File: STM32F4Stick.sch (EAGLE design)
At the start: 46 parts, among them U1 MIC5219 3.3V, U2 USD-SOCKETNEW

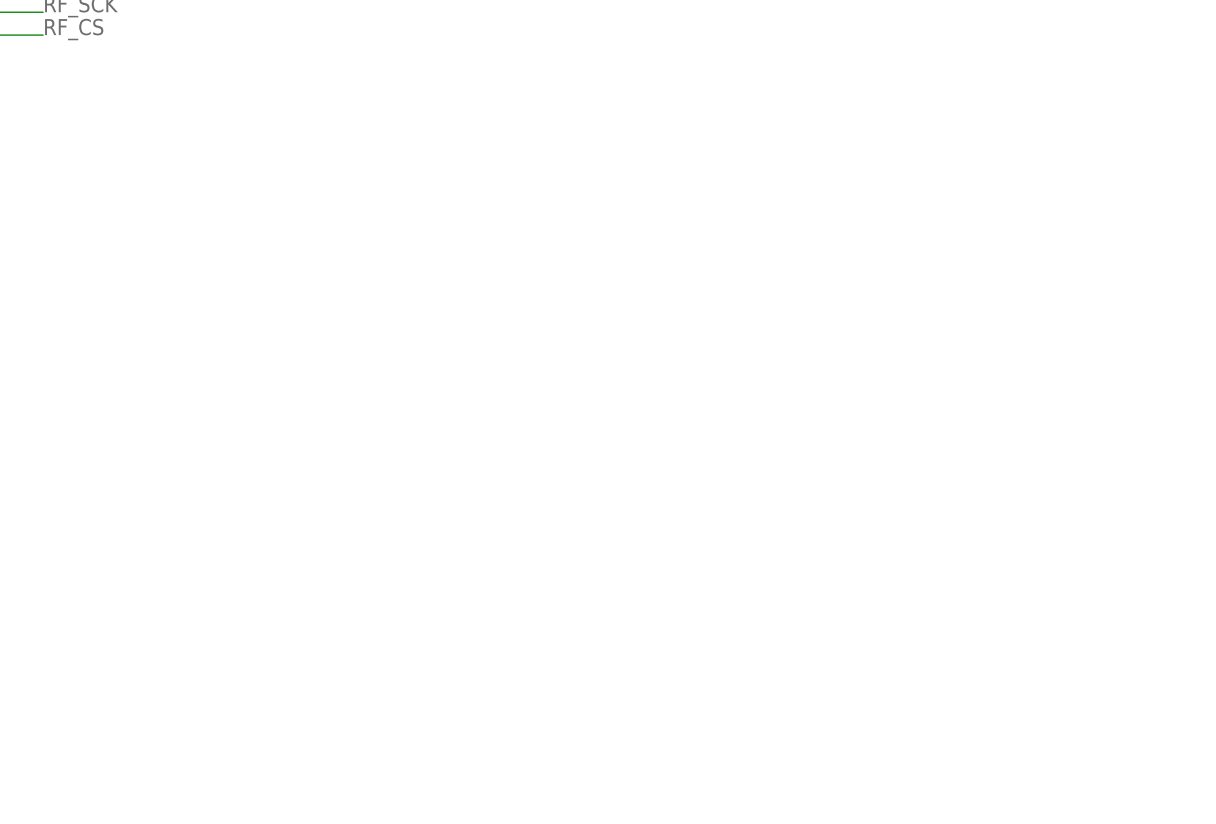
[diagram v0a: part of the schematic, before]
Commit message: version 3 still in development. playing with mpu6050/9150 module to see if one can fit
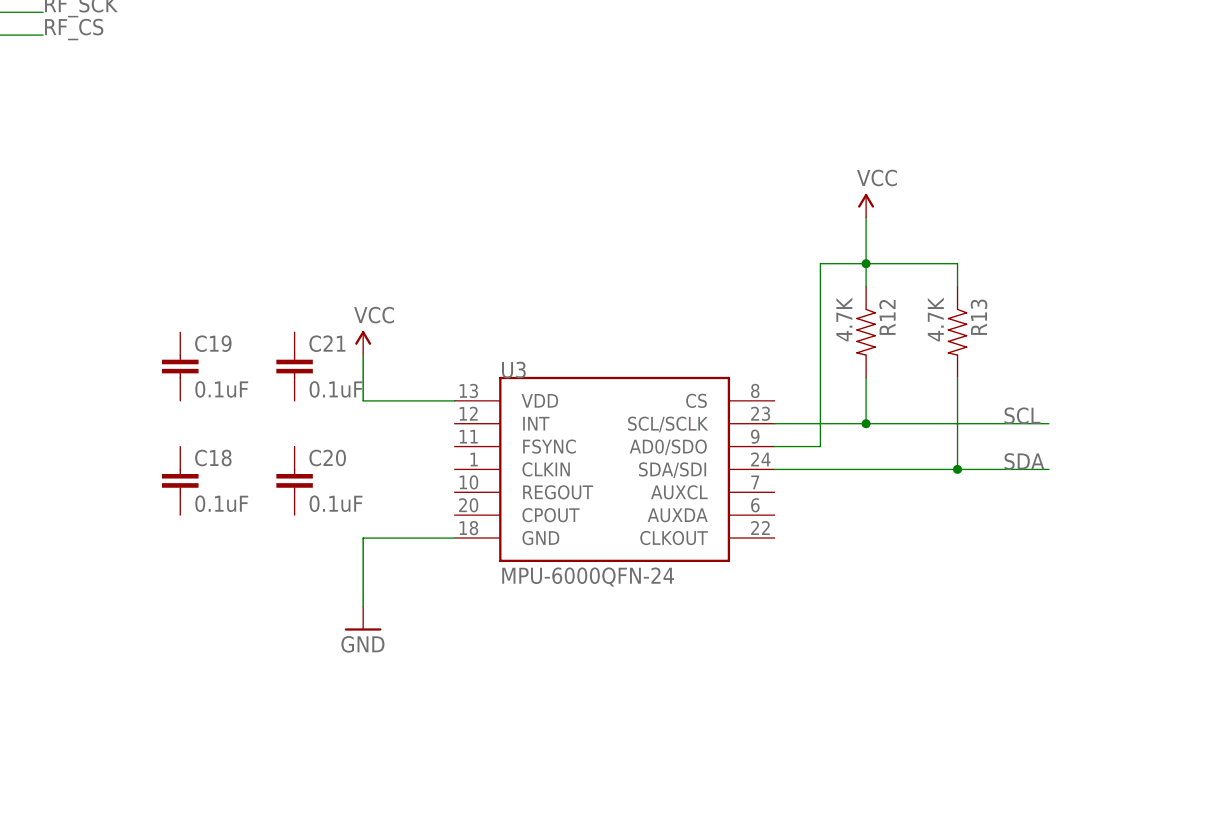
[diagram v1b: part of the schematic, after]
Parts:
- added C18, C19, C20, C21: 0.1uF, SparkFun-Capacitors:0.1UF-25V-5%(0603)
- added R12, R13: 4.7K, SparkFun-Resistors:1KOHM1/10W1%(0603)
- added U3: MPU-6000QFN-24, SparkFun-Sensors:MPU-6000QFN-24
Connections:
- new net SCL: R12.2, U3.SCL/SCLK
- new net SDA: R13.2, U3.SDA/SDI
- net GND: now also U3.GND
- net VCC: now also R12.1, R13.1, U3.AD0/SDO, U3.VDD
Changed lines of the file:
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@@
 <part name="GND19" library="SparkFun-Aesthetics" deviceset="GND" device=""/>
 <part name="C17" library="SparkFun-Capacitors" deviceset="4.7UF-6.3V-10%(0603)" device="0603" value="4.7uF"/>
+<part name="U3" library="SparkFun-Sensors" deviceset="MPU-6000" device="QFN-24"/>
+<part name="GND20" library="SparkFun-Aesthetics" deviceset="GND" device=""/>
+<part name="SUPPLY11" library="SparkFun-Aesthetics" deviceset="VCC" device=""/>
+<part name="C18" library="SparkFun-Capacitors" deviceset="0.1UF-25V-5%(0603)" device="" value="0.1uF"/>
+<part name="C19" library="SparkFun-Capacitors" deviceset="0.1UF-25V-5%(0603)" device="" value="0.1uF"/>
+<part name="C20" library="SparkFun-Capacitors" deviceset="0.1UF-25V-5%(0603)" device="" value="0.1uF"/>
+<part name="C21" library="SparkFun-Capacitors" deviceset="0.1UF-25V-5%(0603)" device="" value="0.1uF"/>
+<part name="R12" library="SparkFun-Resistors" deviceset="1KOHM1/10W1%(0603)" device="" value="4.7K"/>
+<part name="R13" library="SparkFun-Resistors" deviceset="1KOHM1/10W1%(0603)" device="" value="4.7K"/>
+<part name="SUPPLY12" library="SparkFun-Aesthetics" deviceset="VCC" device=""/>
 </parts>
 <sheets>
@@
 <instance part="GND19" gate="1" x="129.54" y="147.32"/>
 <instance part="C17" gate="G$1" x="129.54" y="157.48"/>
+<instance part="U3" gate="G$1" x="297.18" y="114.3"/>
+<instance part="GND20" gate="1" x="269.24" y="96.52"/>
+<instance part="SUPPLY11" gate="G$1" x="269.24" y="127"/>
+<instance part="C18" gate="G$1" x="248.92" y="111.76"/>
+<instance part="C19" gate="G$1" x="248.92" y="124.46"/>
+<instance part="C20" gate="G$1" x="261.62" y="111.76"/>
+<instance part="C21" gate="G$1" x="261.62" y="124.46"/>
+<instance part="R12" gate="G$1" x="325.12" y="129.54" rot="R270"/>
+<instance part="R13" gate="G$1" x="335.28" y="129.54" rot="R270"/>
+<instance part="SUPPLY12" gate="G$1" x="325.12" y="142.24"/>
 </instances>
 <busses>
@@
 <junction x="182.88" y="48.26"/>
 </segment>
+<segment>
+<pinref part="SUPPLY11" gate="G$1" pin="VCC"/>
+<wire x1="269.24" y1="127" x2="269.24" y2="121.92" width="0.1524" layer="91"/>
+<pinref part="U3" gate="G$1" pin="VDD"/>
+<wire x1="269.24" y1="121.92" x2="279.4" y2="121.92" width="0.1524" layer="91"/>
+</segment>
+<segment>
+<pinref part="R13" gate="G$1" pin="1"/>
+<wire x1="335.28" y1="134.62" x2="335.28" y2="137.16" width="0.1524" layer="91"/>
+<wire x1="335.28" y1="137.16" x2="325.12" y2="137.16" width="0.1524" layer="91"/>
+<pinref part="SUPPLY12" gate="G$1" pin="VCC"/>
+<wire x1="325.12" y1="137.16" x2="325.12" y2="142.24" width="0.1524" layer="91"/>
+<pinref part="R12" gate="G$1" pin="1"/>
+<wire x1="325.12" y1="134.62" x2="325.12" y2="137.16" width="0.1524" layer="91"/>
+<pinref part="U3" gate="G$1" pin="AD0/SDO"/>
+<wire x1="314.96" y1="116.84" x2="320.04" y2="116.84" width="0.1524" layer="91"/>
+<wire x1="320.04" y1="116.84" x2="320.04" y2="137.16" width="0.1524" layer="91"/>
+<wire x1="320.04" y1="137.16" x2="325.12" y2="137.16" width="0.1524" layer="91"/>
+<junction x="325.12" y="137.16"/>
+</segment>
 </net>
 <net name="GND" class="0">
@@
 <wire x1="129.54" y1="154.94" x2="129.54" y2="149.86" width="0.1524" layer="91"/>
 </segment>
+<segment>
+<pinref part="U3" gate="G$1" pin="GND"/>
+<wire x1="279.4" y1="106.68" x2="269.24" y2="106.68" width="0.1524" layer="91"/>
+<pinref part="GND20" gate="1" pin="GND"/>
+<wire x1="269.24" y1="106.68" x2="269.24" y2="99.06" width="0.1524" layer="91"/>
+</segment>
 </net>
 <net name="N$10" class="0">
@@
 </segment>
 </net>
+<net name="SCL" class="0">
+<segment>
+<pinref part="U3" gate="G$1" pin="SCL/SCLK"/>
+<wire x1="314.96" y1="119.38" x2="325.12" y2="119.38" width="0.1524" layer="91"/>
+<pinref part="R12" gate="G$1" pin="2"/>
+<wire x1="325.12" y1="119.38" x2="325.12" y2="124.46" width="0.1524" layer="91"/>
+<wire x1="325.12" y1="119.38" x2="345.44" y2="119.38" width="0.1524" layer="91"/>
+<label x="340.36" y="119.38" size="1.778" layer="95"/>
+<junction x="325.12" y="119.38"/>
+</segment>
+</net>
+<net name="SDA" class="0">
+<segment>
+<pinref part="U3" gate="G$1" pin="SDA/SDI"/>
+<wire x1="314.96" y1="114.3" x2="335.28" y2="114.3" width="0.1524" layer="91"/>
+<pinref part="R13" gate="G$1" pin="2"/>
+<wire x1="335.28" y1="114.3" x2="335.28" y2="124.46" width="0.1524" layer="91"/>
+<wire x1="335.28" y1="114.3" x2="345.44" y2="114.3" width="0.1524" layer="91"/>
+<label x="340.36" y="114.3" size="1.778" layer="95"/>
+<junction x="335.28" y="114.3"/>
+</segment>
+</net>
